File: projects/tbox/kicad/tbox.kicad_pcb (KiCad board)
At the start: 4 copper layers, 300 x 250 mm, 0 parts

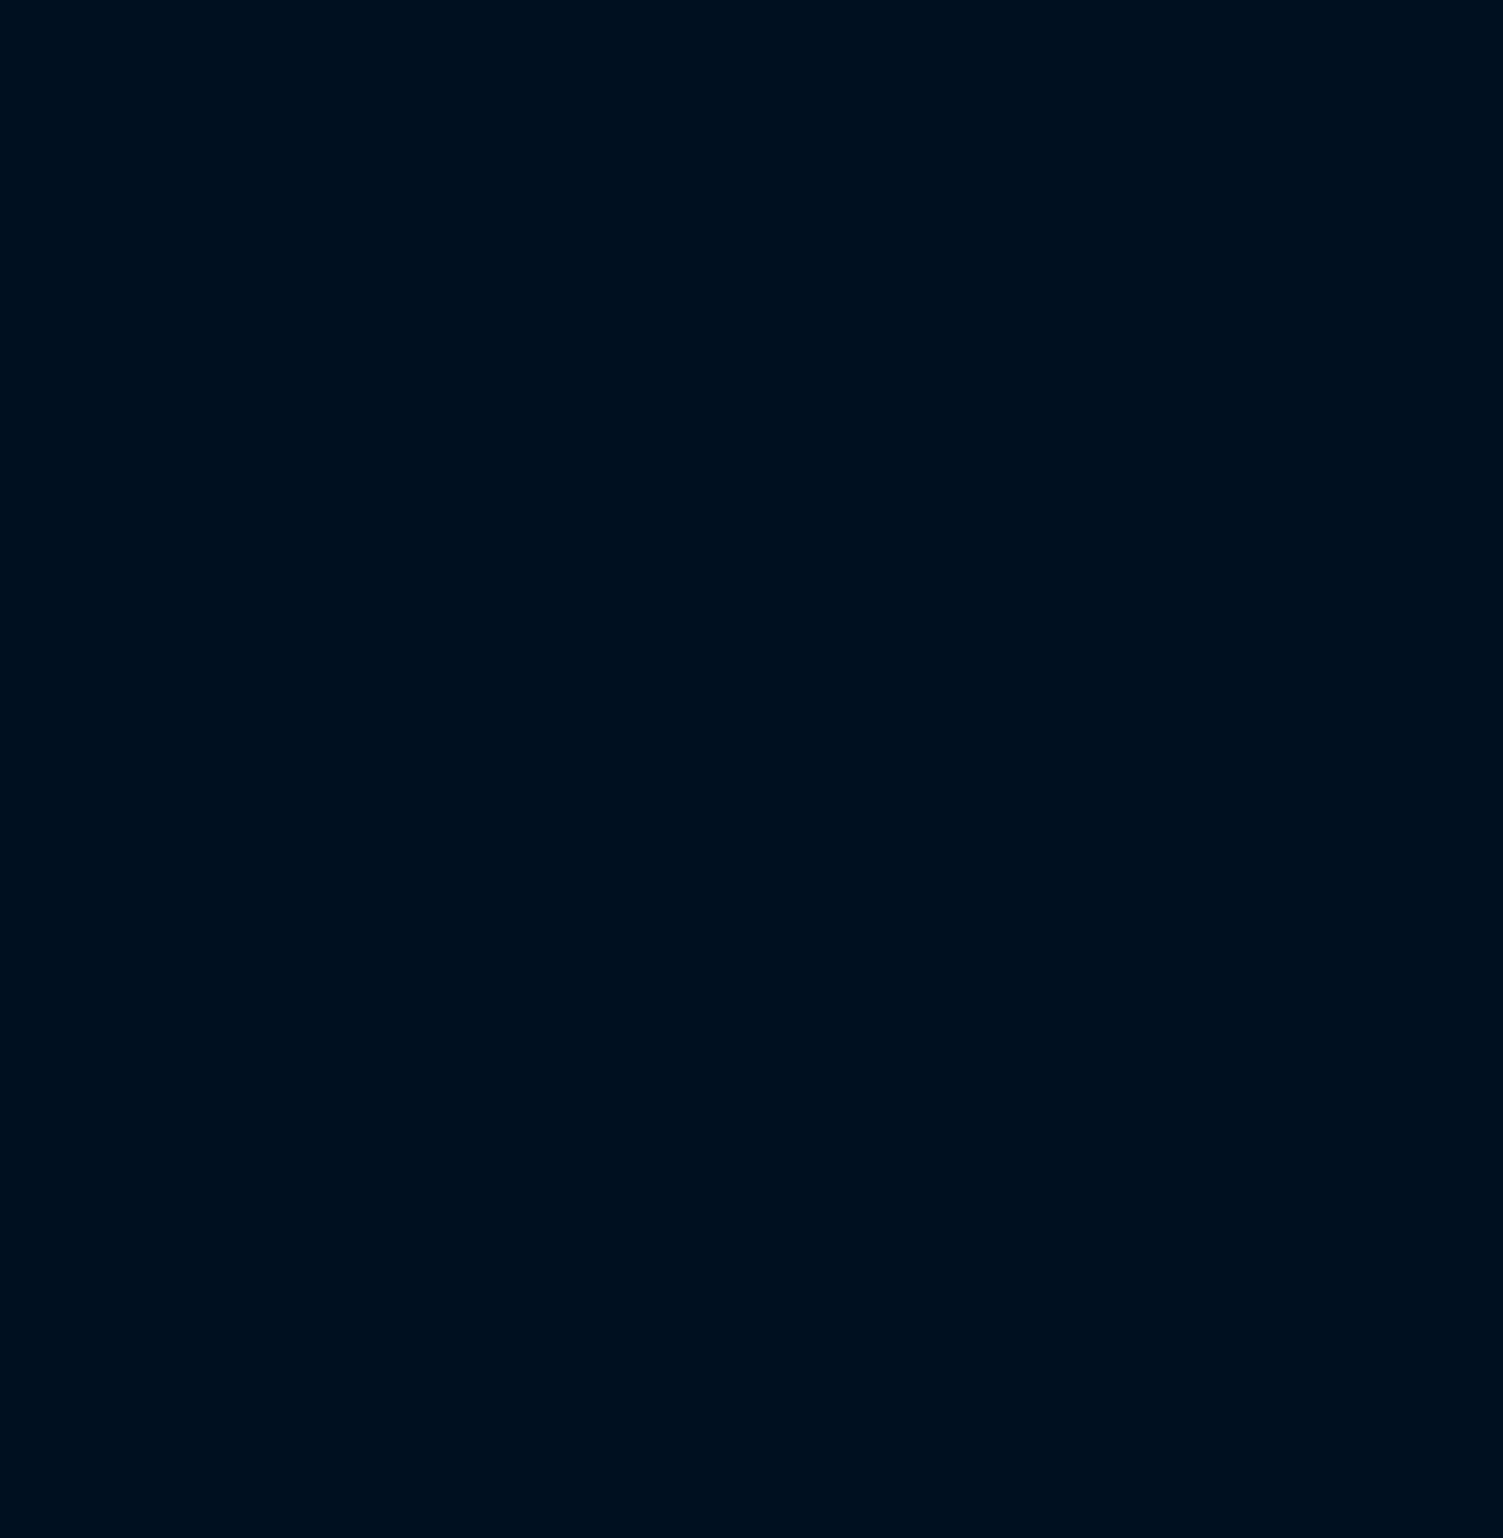
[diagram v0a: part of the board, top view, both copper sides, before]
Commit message: Footprints pulled into the panel PCB (Update PCB from Schematic)
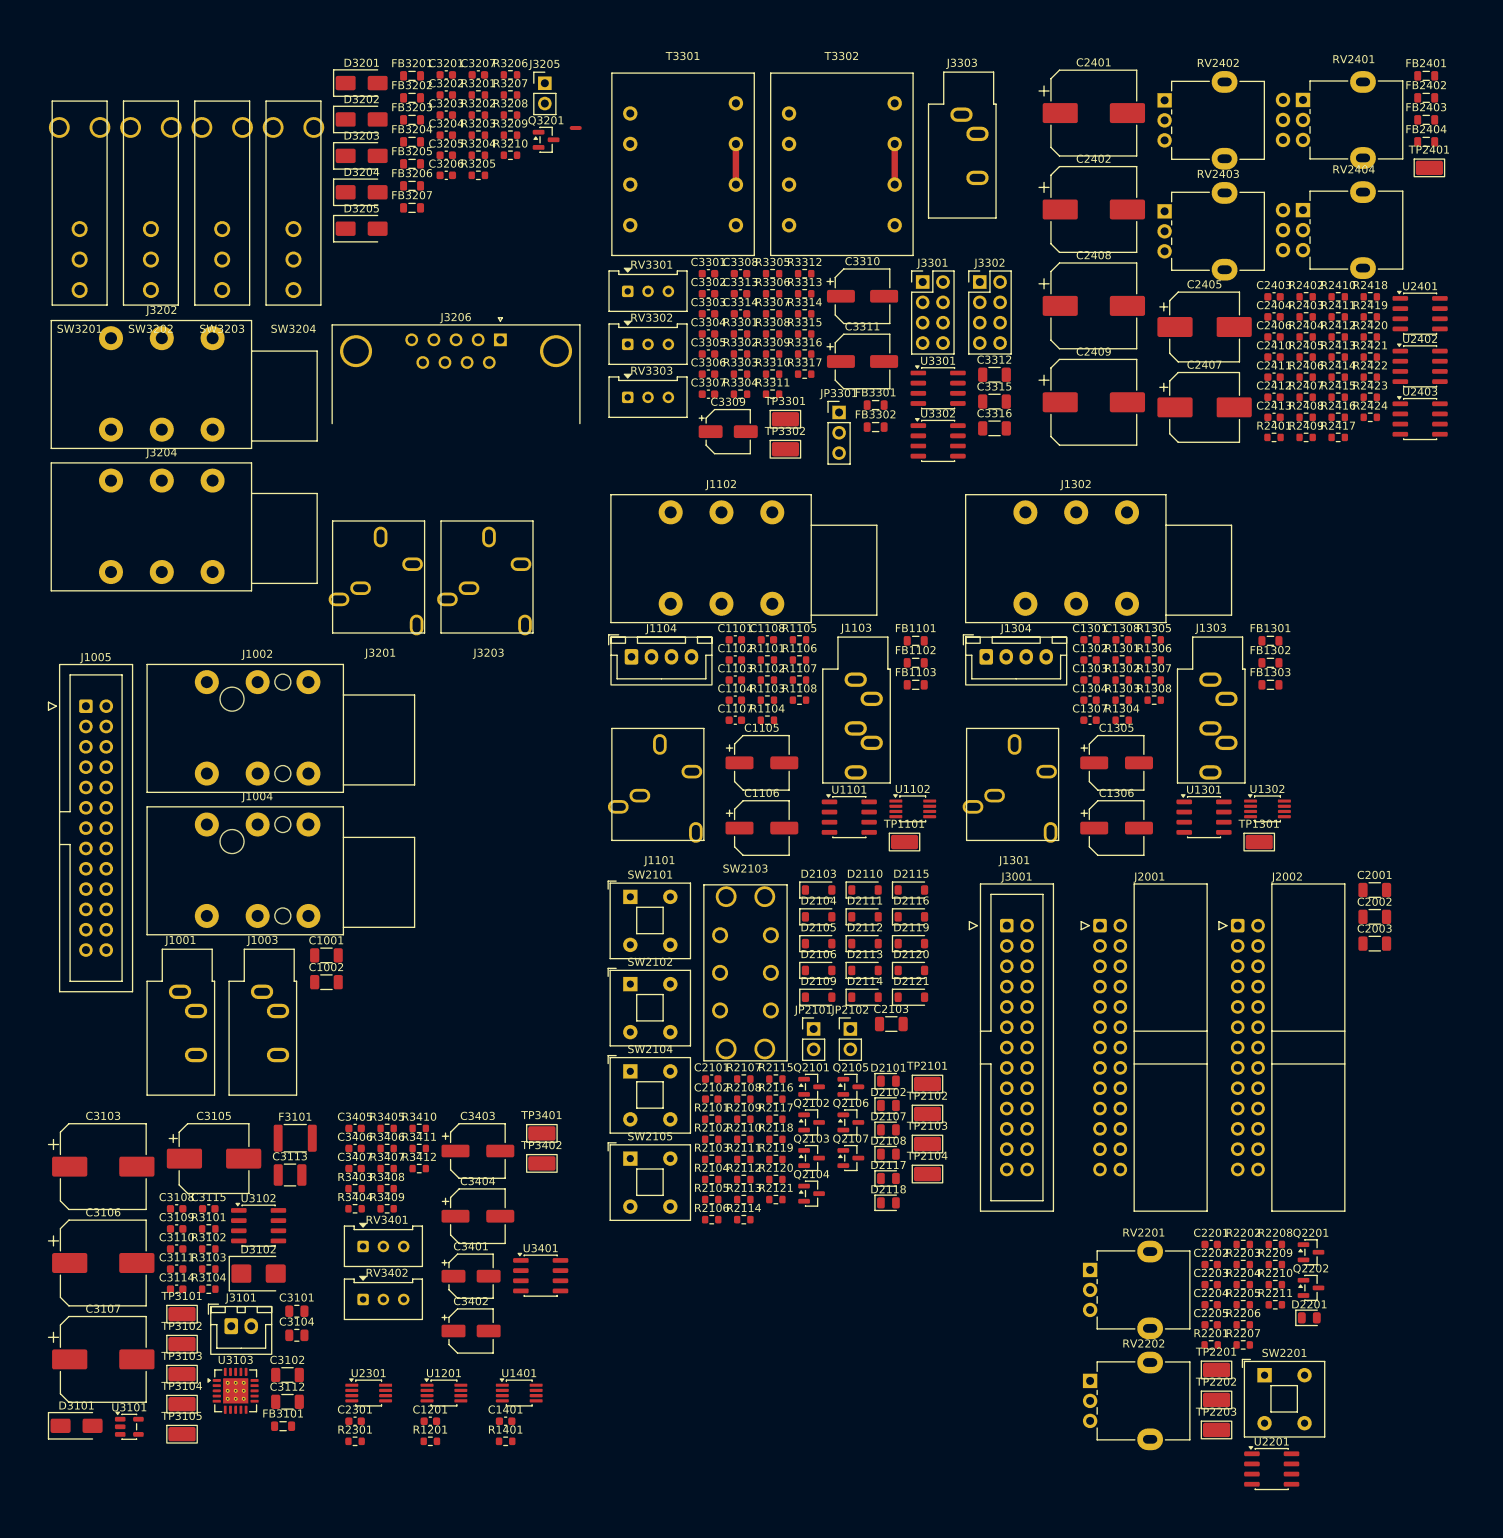
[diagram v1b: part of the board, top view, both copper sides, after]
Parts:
- added C1001: 10u, Capacitor_SMD:C_1206_3216Metric, F.Cu at (92.1, 162.8)
- added C1002: 10u, Capacitor_SMD:C_1206_3216Metric, F.Cu at (92.1, 166.2)
- added C1101: 1n, Capacitor_SMD:C_0603_1608Metric, F.Cu at (143.2, 123.4)
- added C1102: 100n, Capacitor_SMD:C_0603_1608Metric, F.Cu at (143.2, 125.9)
- added C1103: 1u, Capacitor_SMD:C_0603_1608Metric, F.Cu at (143.2, 128.4)
- added C1104: 100p, Capacitor_SMD:C_0603_1608Metric, F.Cu at (143.2, 130.9)
- added C1105: 47u, Capacitor_SMD:CP_Elec_6.3x5.4, F.Cu at (146.5, 138.7)
- added C1106: 47u, Capacitor_SMD:CP_Elec_6.3x5.4, F.Cu at (146.5, 146.9)
- added C1107: 100n, Capacitor_SMD:C_0603_1608Metric, F.Cu at (143.2, 133.4)
- added C1108: 100n, Capacitor_SMD:C_0603_1608Metric, F.Cu at (147.2, 123.4)
- added C1201: 100n, Capacitor_SMD:C_0603_1608Metric, F.Cu at (105.0, 221.0)
- added C1301: 1n, Capacitor_SMD:C_0603_1608Metric, F.Cu at (187.5, 123.4)
- added C1302: 100n, Capacitor_SMD:C_0603_1608Metric, F.Cu at (187.5, 125.9)
- added C1303: 1u, Capacitor_SMD:C_0603_1608Metric, F.Cu at (187.5, 128.4)
- added C1304: 100p, Capacitor_SMD:C_0603_1608Metric, F.Cu at (187.5, 130.9)
- added C1305: 47u, Capacitor_SMD:CP_Elec_6.3x5.4, F.Cu at (190.8, 138.7)
- added C1306: 47u, Capacitor_SMD:CP_Elec_6.3x5.4, F.Cu at (190.8, 146.9)
- added C1307: 100n, Capacitor_SMD:C_0603_1608Metric, F.Cu at (187.5, 133.4)
- added C1308: 100n, Capacitor_SMD:C_0603_1608Metric, F.Cu at (191.5, 123.4)
- added C1401: 100n, Capacitor_SMD:C_0603_1608Metric, F.Cu at (114.5, 221.0)
- added C2001: 10u, Capacitor_SMD:C_1206_3216Metric, F.Cu at (223.1, 154.6)
- added C2002: 10u, Capacitor_SMD:C_1206_3216Metric, F.Cu at (223.1, 158.0)
- added C2003: 10u, Capacitor_SMD:C_1206_3216Metric, F.Cu at (223.1, 161.3)
- added C2101: 100n, Capacitor_SMD:C_0603_1608Metric, F.Cu at (140.2, 178.3)
- added C2102: 100n, Capacitor_SMD:C_0603_1608Metric, F.Cu at (140.2, 180.8)
- added C2103: 10u, Capacitor_SMD:C_1206_3216Metric, F.Cu at (162.7, 171.4)
- added C2201: 1u, Capacitor_SMD:C_0603_1608Metric, F.Cu at (202.6, 199.0)
- added C2202: 1u, Capacitor_SMD:C_0603_1608Metric, F.Cu at (202.6, 201.5)
- added C2203: 100n, Capacitor_SMD:C_0603_1608Metric, F.Cu at (202.6, 204.0)
- added C2204: 47p, Capacitor_SMD:C_0603_1608Metric, F.Cu at (202.6, 206.5)
- added C2205: 100n, Capacitor_SMD:C_0603_1608Metric, F.Cu at (202.6, 209.0)
- added C2301: 100n, Capacitor_SMD:C_0603_1608Metric, F.Cu at (95.6, 221.0)
- added C2401: 470u, Capacitor_SMD:CP_Elec_10x10.5, F.Cu at (188.0, 57.5)
- added C2402: 470u, Capacitor_SMD:CP_Elec_10x10.5, F.Cu at (188.0, 69.6)
- added C2403: 10n, Capacitor_SMD:C_0603_1608Metric, F.Cu at (210.5, 80.5)
- added C2404: 10n, Capacitor_SMD:C_0603_1608Metric, F.Cu at (210.5, 83.0)
- added C2405: 220u, Capacitor_SMD:CP_Elec_8x10.5, F.Cu at (201.8, 84.3)
- added C2406: 100n, Capacitor_SMD:C_0603_1608Metric, F.Cu at (210.5, 85.5)
- added C2407: 220u, Capacitor_SMD:CP_Elec_8x10.5, F.Cu at (201.8, 94.3)
- added C2408: 470u, Capacitor_SMD:CP_Elec_10x10.5, F.Cu at (188.0, 81.6)
- added C2409: 470u, Capacitor_SMD:CP_Elec_10x10.5, F.Cu at (188.0, 93.7)
- added C2410: 100n, Capacitor_SMD:C_0603_1608Metric, F.Cu at (210.5, 88.0)
- added C2411: 10n, Capacitor_SMD:C_0603_1608Metric, F.Cu at (210.5, 90.5)
- added C2412: 10n, Capacitor_SMD:C_0603_1608Metric, F.Cu at (210.5, 93.0)
- added C2413: 100n, Capacitor_SMD:C_0603_1608Metric, F.Cu at (210.5, 95.6)
- added C3101: 4u7, Capacitor_SMD:C_0805_2012Metric, F.Cu at (88.4, 207.3)
- added C3102: 10u, Capacitor_SMD:C_1206_3216Metric, F.Cu at (87.2, 215.3)
- added C3103: 220u 35V, Capacitor_SMD:CP_Elec_10x10.5, F.Cu at (64.2, 189.2)
- added C3104: 4u7, Capacitor_SMD:C_0805_2012Metric, F.Cu at (88.4, 210.3)
- added C3105: 220u, Capacitor_SMD:CP_Elec_8x10.5, F.Cu at (78.0, 188.2)
- added C3106: 220u 35V, Capacitor_SMD:CP_Elec_10x10.5, F.Cu at (64.2, 201.3)
- added C3107: 470u, Capacitor_SMD:CP_Elec_10x10.5, F.Cu at (64.2, 213.3)
- added C3108: 100n, Capacitor_SMD:C_0603_1608Metric, F.Cu at (73.3, 194.5)
- added C3109: 100n, Capacitor_SMD:C_0603_1608Metric, F.Cu at (73.3, 197.0)
- added C3110: 1n, Capacitor_SMD:C_0603_1608Metric, F.Cu at (73.3, 199.5)
- added C3111: 100n, Capacitor_SMD:C_0603_1608Metric, F.Cu at (73.3, 202.0)
- added C3112: 10u, Capacitor_SMD:C_1206_3216Metric, F.Cu at (87.2, 218.6)
- added C3113: 47u X7R, Capacitor_SMD:C_1210_3225Metric, F.Cu at (87.5, 190.3)
- added C3114: 1u, Capacitor_SMD:C_0603_1608Metric, F.Cu at (73.3, 204.5)
- added C3115: 100n, Capacitor_SMD:C_0603_1608Metric, F.Cu at (77.3, 194.5)
- added C3201: 10n, Capacitor_SMD:C_0603_1608Metric, F.Cu at (107.0, 52.8)
- added C3202: 10n, Capacitor_SMD:C_0603_1608Metric, F.Cu at (107.0, 55.3)
- added C3203: 1n, Capacitor_SMD:C_0603_1608Metric, F.Cu at (107.0, 57.8)
- added C3204: 1n, Capacitor_SMD:C_0603_1608Metric, F.Cu at (107.0, 60.3)
- added C3205: 1n, Capacitor_SMD:C_0603_1608Metric, F.Cu at (107.0, 62.8)
- added C3206: 10n, Capacitor_SMD:C_0603_1608Metric, F.Cu at (107.0, 65.3)
- added C3207: 10n, Capacitor_SMD:C_0603_1608Metric, F.Cu at (111.0, 52.8)
- added C3301: 100n, Capacitor_SMD:C_0603_1608Metric, F.Cu at (139.8, 77.6)
- added C3302: 100n, Capacitor_SMD:C_0603_1608Metric, F.Cu at (139.8, 80.1)
- added C3303: 1u, Capacitor_SMD:C_0603_1608Metric, F.Cu at (139.8, 82.6)
- added C3304: 100p, Capacitor_SMD:C_0603_1608Metric, F.Cu at (139.8, 85.1)
- added C3305: 1u, Capacitor_SMD:C_0603_1608Metric, F.Cu at (139.8, 87.6)
- added C3306: 1u, Capacitor_SMD:C_0603_1608Metric, F.Cu at (139.8, 90.2)
- added C3307: 100p, Capacitor_SMD:C_0603_1608Metric, F.Cu at (139.8, 92.7)
- added C3308: 100p, Capacitor_SMD:C_0603_1608Metric, F.Cu at (143.8, 77.6)
- added C3309: 10u, Capacitor_SMD:CP_Elec_5x5.4, F.Cu at (142.3, 97.3)
- added C3310: 100u, Capacitor_SMD:CP_Elec_6.3x7.7, F.Cu at (159.1, 80.4)
- added C3311: 100u, Capacitor_SMD:CP_Elec_6.3x7.7, F.Cu at (159.1, 88.6)
- added C3312: 10u NP, Capacitor_SMD:C_1206_3216Metric, F.Cu at (175.6, 90.2)
- added C3313: 1n, Capacitor_SMD:C_0603_1608Metric, F.Cu at (143.8, 80.1)
- added C3314: 1n, Capacitor_SMD:C_0603_1608Metric, F.Cu at (143.8, 82.6)
- added C3315: 10u NP, Capacitor_SMD:C_1206_3216Metric, F.Cu at (175.6, 93.6)
- added C3316: 10u NP, Capacitor_SMD:C_1206_3216Metric, F.Cu at (175.6, 96.9)
- added C3401: 10u, Capacitor_SMD:CP_Elec_5x5.4, F.Cu at (110.1, 202.9)
- added C3402: 10u, Capacitor_SMD:CP_Elec_5x5.4, F.Cu at (110.1, 209.8)
- added C3403: 47u, Capacitor_SMD:CP_Elec_6.3x5.4, F.Cu at (111.0, 187.3)
- added C3404: 47u, Capacitor_SMD:CP_Elec_6.3x5.4, F.Cu at (111.0, 195.4)
- added C3405: 100p, Capacitor_SMD:C_0603_1608Metric, F.Cu at (95.6, 184.4)
- added C3406: 100p, Capacitor_SMD:C_0603_1608Metric, F.Cu at (95.6, 187.0)
- added C3407: 100n, Capacitor_SMD:C_0603_1608Metric, F.Cu at (95.6, 189.5)
- added D2101: TX, LED_SMD:LED_0805_2012Metric, F.Cu at (162.3, 178.5)
- added D2102: PTT A, LED_SMD:LED_0805_2012Metric, F.Cu at (162.3, 181.6)
- added D2103: 1N4148W, Diode_SMD:D_SOD-123, F.Cu at (153.6, 154.6)
- added D2104: 1N4148W, Diode_SMD:D_SOD-123, F.Cu at (153.6, 158.0)
- added D2105: 1N4148W, Diode_SMD:D_SOD-123, F.Cu at (153.6, 161.3)
- added D2106: 1N4148W, Diode_SMD:D_SOD-123, F.Cu at (153.6, 164.7)
- added D2107: PTT B, LED_SMD:LED_0805_2012Metric, F.Cu at (162.3, 184.6)
- added D2108: MUTE A, LED_SMD:LED_0805_2012Metric, F.Cu at (162.3, 187.7)
- added D2109: 1N4148W, Diode_SMD:D_SOD-123, F.Cu at (153.6, 168.0)
- added D2110: 1N4148W, Diode_SMD:D_SOD-123, F.Cu at (159.4, 154.6)
- added D2111: 1N4148W, Diode_SMD:D_SOD-123, F.Cu at (159.4, 158.0)
- added D2112: 1N4148W, Diode_SMD:D_SOD-123, F.Cu at (159.4, 161.3)
- added D2113: 1N4148W, Diode_SMD:D_SOD-123, F.Cu at (159.4, 164.7)
- added D2114: 1N4148W, Diode_SMD:D_SOD-123, F.Cu at (159.4, 168.0)
- added D2115: 1N4148W, Diode_SMD:D_SOD-123, F.Cu at (165.2, 154.6)
- added D2116: 1N4148W, Diode_SMD:D_SOD-123, F.Cu at (165.2, 158.0)
- added D2117: MUTE B, LED_SMD:LED_0805_2012Metric, F.Cu at (162.3, 190.7)
- added D2118: PWR, LED_SMD:LED_0805_2012Metric, F.Cu at (162.3, 193.7)
- added D2119: 1N4148W, Diode_SMD:D_SOD-123, F.Cu at (165.2, 161.3)
- added D2120: 1N4148W, Diode_SMD:D_SOD-123, F.Cu at (165.2, 164.7)
- added D2121: 1N4148W, Diode_SMD:D_SOD-123, F.Cu at (165.2, 168.0)
- added D2201: IC LED, LED_SMD:LED_0805_2012Metric, F.Cu at (214.9, 208.1)
- added D3101: SS34, Diode_SMD:D_SMA, F.Cu at (60.8, 221.6)
- added D3102: SMBJ18A, Diode_SMD:D_SMB, F.Cu at (83.6, 202.6)
- added D3201: SMAJ15CA, Diode_SMD:D_SMA, F.Cu at (96.5, 53.8)
- added D3202: SMAJ15CA, Diode_SMD:D_SMA, F.Cu at (96.5, 58.3)
- added D3203: SMAJ15CA, Diode_SMD:D_SMA, F.Cu at (96.5, 62.9)
- added D3204: SMAJ15A, Diode_SMD:D_SMA, F.Cu at (96.5, 67.4)
- added D3205: SMAJ15A, Diode_SMD:D_SMA, F.Cu at (96.5, 72.0)
- added F3101: PTC 500mA, Fuse:Fuse_1812_4532Metric, F.Cu at (88.2, 185.7)
- added FB1101: 600R, Inductor_SMD:L_0805_2012Metric, F.Cu at (165.7, 123.5)
- added FB1102: 600R, Inductor_SMD:L_0805_2012Metric, F.Cu at (165.7, 126.2)
- added FB1103: 600R, Inductor_SMD:L_0805_2012Metric, F.Cu at (165.7, 129.0)
- added FB1301: 600R, Inductor_SMD:L_0805_2012Metric, F.Cu at (210.1, 123.5)
- added FB1302: 600R, Inductor_SMD:L_0805_2012Metric, F.Cu at (210.1, 126.2)
- added FB1303: 600R, Inductor_SMD:L_0805_2012Metric, F.Cu at (210.1, 129.0)
- added FB2401: 600R, Inductor_SMD:L_0805_2012Metric, F.Cu at (229.5, 52.9)
- added FB2402: 600R, Inductor_SMD:L_0805_2012Metric, F.Cu at (229.5, 55.6)
- added FB2403: 600R, Inductor_SMD:L_0805_2012Metric, F.Cu at (229.5, 58.4)
- added FB2404: 600R, Inductor_SMD:L_0805_2012Metric, F.Cu at (229.5, 61.1)
- added FB3101: 600R, Inductor_SMD:L_0805_2012Metric, F.Cu at (86.6, 221.7)
- added FB3201: 600R, Inductor_SMD:L_0805_2012Metric, F.Cu at (102.8, 52.9)
- added FB3202: 600R, Inductor_SMD:L_0805_2012Metric, F.Cu at (102.8, 55.6)
- added FB3203: 600R, Inductor_SMD:L_0805_2012Metric, F.Cu at (102.8, 58.4)
- added FB3204: 600R, Inductor_SMD:L_0805_2012Metric, F.Cu at (102.8, 61.1)
- added FB3205: 600R, Inductor_SMD:L_0805_2012Metric, F.Cu at (102.8, 63.9)
- added FB3206: 600R, Inductor_SMD:L_0805_2012Metric, F.Cu at (102.8, 66.6)
- added FB3207: 600R, Inductor_SMD:L_0805_2012Metric, F.Cu at (102.8, 69.4)
- added FB3301: 600R, Inductor_SMD:L_0805_2012Metric, F.Cu at (160.7, 94.0)
- added FB3302: 600R, Inductor_SMD:L_0805_2012Metric, F.Cu at (160.7, 96.8)
- added J1001: PHONES A 3.5, Connector_Audio:Jack_3.5mm_CUI_SJ1-3533NG_Horizontal, F.Cu at (73.8, 167.4)
- added J1002: PHONES A 1/4, Connector_Audio:Jack_6.35mm_Neutrik_NRJ6HF-1_Horizontal, F.Cu at (77.1, 128.7)
- added J1003: PHONES B 3.5, Connector_Audio:Jack_3.5mm_CUI_SJ1-3533NG_Horizontal, F.Cu at (84.0, 167.4)
- added J1004: PHONES B 1/4, Connector_Audio:Jack_6.35mm_Neutrik_NRJ6HF-1_Horizontal, F.Cu at (77.1, 146.5)
- added J1005: TO CTRL J2001, Connector_IDC:IDC-Header_2x13_P2.54mm_Vertical, F.Cu at (62.0, 131.7)
- added J1101: MIC 3.5, tbox:Jack_3.5mm_Switchcraft_35RAPCxxH3_Horizontal, F.Cu at (133.7, 134.4)
- added J1102: MIC 1/4, Connector_Audio:Jack_6.35mm_Neutrik_NRJ6HM-1-PRE_Horizontal, F.Cu at (135.1, 107.4)
- added J1103: HEADSET, Connector_Audio:Jack_3.5mm_CUI_SJ1-3535NG_Horizontal, F.Cu at (158.2, 128.3)
- added J1104: SPARE, Connector_JST:JST_XH_B4B-XH-A_1x04_P2.50mm_Vertical, F.Cu at (130.2, 125.5)
- added J1301: MIC 3.5, tbox:Jack_3.5mm_Switchcraft_35RAPCxxH3_Horizontal, F.Cu at (178.1, 134.4)
- added J1302: MIC 1/4, Connector_Audio:Jack_6.35mm_Neutrik_NRJ6HM-1-PRE_Horizontal, F.Cu at (179.4, 107.4)
- added J1303: HEADSET, Connector_Audio:Jack_3.5mm_CUI_SJ1-3535NG_Horizontal, F.Cu at (202.6, 128.3)
- added J1304: SPARE, Connector_JST:JST_XH_B4B-XH-A_1x04_P2.50mm_Vertical, F.Cu at (174.5, 125.5)
- added J2001: TO FRONT J1005, Connector_IDC:IDC-Header_2x13_P2.54mm_Horizontal, F.Cu at (188.8, 159.1)
- added J2002: TO REAR J3001, Connector_IDC:IDC-Header_2x13_P2.54mm_Horizontal, F.Cu at (206.0, 159.1)
- added J3001: TO CTRL J2002, Connector_IDC:IDC-Header_2x13_P2.54mm_Vertical, F.Cu at (177.1, 159.1)
- added J3101: PWR IN (panel Powerpole), Connector_JST:JST_XH_B2B-XH-A_1x02_P2.50mm_Vertical, F.Cu at (80.2, 209.2)
- added J3201: PTT A 3.5, tbox:Jack_3.5mm_Switchcraft_35RAPCxxH3_Horizontal, F.Cu at (98.8, 108.5)
- added J3202: PTT A 1/4, Connector_Audio:Jack_6.35mm_Neutrik_NRJ6HM-1-PRE_Horizontal, F.Cu at (65.1, 85.7)
- added J3203: PTT B 3.5, tbox:Jack_3.5mm_Switchcraft_35RAPCxxH3_Horizontal, F.Cu at (112.4, 108.5)
- added J3204: PTT B 1/4, Connector_Audio:Jack_6.35mm_Neutrik_NRJ6HM-1-PRE_Horizontal, F.Cu at (65.1, 103.5)
- added J3205: CW SPARE, Connector_PinHeader_2.54mm:PinHeader_1x02_P2.54mm_Vertical, F.Cu at (119.4, 53.8)
- added J3206: RIG DE-9, Connector_Dsub:DSUB-9_Socket_Horizontal_P2.77x2.84mm_EdgePinOffset7.70mm_Housed_MountingHolesOffset9.12mm, F.Cu at (113.8, 85.9)
- added J3301: LINE L SRC, Connector_PinHeader_2.54mm:PinHeader_2x04_P2.54mm_Vertical, F.Cu at (166.6, 78.6)
- added J3302: LINE R SRC, Connector_PinHeader_2.54mm:PinHeader_2x04_P2.54mm_Vertical, F.Cu at (173.7, 78.6)
- added J3303: LINE OUT, Connector_Audio:Jack_3.5mm_CUI_SJ1-3533NG_Horizontal, F.Cu at (171.4, 57.7)
- added JP2101: PTT GATE, Connector_PinHeader_2.54mm:PinHeader_1x02_P2.54mm_Vertical, F.Cu at (153.0, 172.0)
- added JP2102: PTT GATE, Connector_PinHeader_2.54mm:PinHeader_1x02_P2.54mm_Vertical, F.Cu at (157.5, 172.0)
- added JP3301: MIC/LINE, Connector_PinHeader_2.54mm:PinHeader_1x03_P2.54mm_Vertical, F.Cu at (156.1, 94.9)
- added NT3201: CHASSIS-GND tie, NetTie:NetTie-2_SMD_Pad0.5mm, F.Cu at (123.2, 59.4)
- added Q2101: 2N7002, Package_TO_SOT_SMD:SOT-23, F.Cu at (152.7, 179.2)
- added Q2102: 2N7002, Package_TO_SOT_SMD:SOT-23, F.Cu at (152.7, 183.7)
- added Q2103: 2N7002, Package_TO_SOT_SMD:SOT-23, F.Cu at (152.7, 188.1)
- added Q2104: 2N7002, Package_TO_SOT_SMD:SOT-23, F.Cu at (152.7, 192.6)
- added Q2105: 2N7002, Package_TO_SOT_SMD:SOT-23, F.Cu at (157.6, 179.2)
- added Q2106: 2N7002, Package_TO_SOT_SMD:SOT-23, F.Cu at (157.6, 183.7)
- added Q2107: 2N7002, Package_TO_SOT_SMD:SOT-23, F.Cu at (157.6, 188.1)
- added Q2201: MMBT3904, Package_TO_SOT_SMD:SOT-23, F.Cu at (215.1, 199.9)
- added Q2202: 2N7002, Package_TO_SOT_SMD:SOT-23, F.Cu at (215.1, 204.4)
- added Q3201: 2N7002, Package_TO_SOT_SMD:SOT-23, F.Cu at (119.5, 60.9)
- added R1101: 2k2, Resistor_SMD:R_0603_1608Metric, F.Cu at (147.2, 125.9)
- added R1102: 47k, Resistor_SMD:R_0603_1608Metric, F.Cu at (147.2, 128.4)
- added R1103: 100R, Resistor_SMD:R_0603_1608Metric, F.Cu at (147.2, 130.9)
- added R1104: 1k1, Resistor_SMD:R_0603_1608Metric, F.Cu at (147.2, 133.4)
- added R1105: 10k, Resistor_SMD:R_0603_1608Metric, F.Cu at (151.2, 123.4)
- added R1106: 1k1, Resistor_SMD:R_0603_1608Metric, F.Cu at (151.2, 125.9)
- added R1107: 10k, Resistor_SMD:R_0603_1608Metric, F.Cu at (151.2, 128.4)
- added R1108: 100k, Resistor_SMD:R_0603_1608Metric, F.Cu at (151.2, 130.9)
- added R1201: 1M, Resistor_SMD:R_0603_1608Metric, F.Cu at (105.0, 223.6)
- added R1301: 2k2, Resistor_SMD:R_0603_1608Metric, F.Cu at (191.5, 125.9)
- added R1302: 47k, Resistor_SMD:R_0603_1608Metric, F.Cu at (191.5, 128.4)
- added R1303: 100R, Resistor_SMD:R_0603_1608Metric, F.Cu at (191.5, 130.9)
- added R1304: 1k1, Resistor_SMD:R_0603_1608Metric, F.Cu at (191.5, 133.4)
- added R1305: 10k, Resistor_SMD:R_0603_1608Metric, F.Cu at (195.5, 123.4)
- added R1306: 1k1, Resistor_SMD:R_0603_1608Metric, F.Cu at (195.5, 125.9)
- added R1307: 10k, Resistor_SMD:R_0603_1608Metric, F.Cu at (195.5, 128.4)
- added R1308: 100k, Resistor_SMD:R_0603_1608Metric, F.Cu at (195.5, 130.9)
- added R1401: 1M, Resistor_SMD:R_0603_1608Metric, F.Cu at (114.5, 223.6)
- added R2101: 10k, Resistor_SMD:R_0603_1608Metric, F.Cu at (140.2, 183.3)
- added R2102: 680R, Resistor_SMD:R_0603_1608Metric, F.Cu at (140.2, 185.8)
- added R2103: 10k, Resistor_SMD:R_0603_1608Metric, F.Cu at (140.2, 188.3)
- added R2104: 1k, Resistor_SMD:R_0603_1608Metric, F.Cu at (140.2, 190.8)
- added R2105: 1k, Resistor_SMD:R_0603_1608Metric, F.Cu at (140.2, 193.3)
- added R2106: 2k2, Resistor_SMD:R_0603_1608Metric, F.Cu at (140.2, 195.8)
- added R2107: 10k, Resistor_SMD:R_0603_1608Metric, F.Cu at (144.2, 178.3)
- added R2108: 10k, Resistor_SMD:R_0603_1608Metric, F.Cu at (144.2, 180.8)
- added R2109: 10k, Resistor_SMD:R_0603_1608Metric, F.Cu at (144.2, 183.3)
- added R2110: 2k2, Resistor_SMD:R_0603_1608Metric, F.Cu at (144.2, 185.8)
- added R2111: 2k2, Resistor_SMD:R_0603_1608Metric, F.Cu at (144.2, 188.3)
- added R2112: 2k2, Resistor_SMD:R_0603_1608Metric, F.Cu at (144.2, 190.8)
- added R2113: 10k, Resistor_SMD:R_0603_1608Metric, F.Cu at (144.2, 193.3)
- added R2114: 2k2, Resistor_SMD:R_0603_1608Metric, F.Cu at (144.2, 195.8)
- added R2115: 1k, Resistor_SMD:R_0603_1608Metric, F.Cu at (148.2, 178.3)
- added R2116: 1k, Resistor_SMD:R_0603_1608Metric, F.Cu at (148.2, 180.8)
- added R2117: 47k, Resistor_SMD:R_0603_1608Metric, F.Cu at (148.2, 183.3)
- added R2118: 10k, Resistor_SMD:R_0603_1608Metric, F.Cu at (148.2, 185.8)
- added R2119: 2k2, Resistor_SMD:R_0603_1608Metric, F.Cu at (148.2, 188.3)
- added R2120: 2k2, Resistor_SMD:R_0603_1608Metric, F.Cu at (148.2, 190.8)
- added R2121: 470k, Resistor_SMD:R_0603_1608Metric, F.Cu at (148.2, 193.3)
- added R2201: 10k, Resistor_SMD:R_0603_1608Metric, F.Cu at (202.6, 211.5)
- added R2202: 10k, Resistor_SMD:R_0603_1608Metric, F.Cu at (206.7, 199.0)
- added R2203: 10k, Resistor_SMD:R_0603_1608Metric, F.Cu at (206.7, 201.5)
- added R2204: 10k, Resistor_SMD:R_0603_1608Metric, F.Cu at (206.7, 204.0)
- added R2205: 20k, Resistor_SMD:R_0603_1608Metric, F.Cu at (206.7, 206.5)
- added R2206: 10k, Resistor_SMD:R_0603_1608Metric, F.Cu at (206.7, 209.0)
- added R2207: 100R, Resistor_SMD:R_0603_1608Metric, F.Cu at (206.7, 211.5)
- added R2208: 10k, Resistor_SMD:R_0603_1608Metric, F.Cu at (210.7, 199.0)
- added R2209: 10k, Resistor_SMD:R_0603_1608Metric, F.Cu at (210.7, 201.5)
- added R2210: 2k2, Resistor_SMD:R_0603_1608Metric, F.Cu at (210.7, 204.0)
- added R2211: 100k, Resistor_SMD:R_0603_1608Metric, F.Cu at (210.7, 206.5)
- added R2301: 1M, Resistor_SMD:R_0603_1608Metric, F.Cu at (95.6, 223.6)
- added R2401: 10k, Resistor_SMD:R_0603_1608Metric, F.Cu at (210.5, 98.1)
- added R2402: 10k, Resistor_SMD:R_0603_1608Metric, F.Cu at (214.5, 80.5)
- added R2403: 10k, Resistor_SMD:R_0603_1608Metric, F.Cu at (214.5, 83.0)
- added R2404: 10k, Resistor_SMD:R_0603_1608Metric, F.Cu at (214.5, 85.5)
- added R2405: 10k, Resistor_SMD:R_0603_1608Metric, F.Cu at (214.5, 88.0)
- added R2406: 10k, Resistor_SMD:R_0603_1608Metric, F.Cu at (214.5, 90.5)
- added R2407: 150k, Resistor_SMD:R_0603_1608Metric, F.Cu at (214.5, 93.0)
- added R2408: 150k, Resistor_SMD:R_0603_1608Metric, F.Cu at (214.5, 95.6)
- added R2409: 10R, Resistor_SMD:R_0603_1608Metric, F.Cu at (214.5, 98.1)
- added R2410: 10R, Resistor_SMD:R_0603_1608Metric, F.Cu at (218.5, 80.5)
- added R2411: 4k7, Resistor_SMD:R_0603_1608Metric, F.Cu at (218.5, 83.0)
- added R2412: 4k7, Resistor_SMD:R_0603_1608Metric, F.Cu at (218.5, 85.5)
- added R2413: 10k, Resistor_SMD:R_0603_1608Metric, F.Cu at (218.5, 88.0)
- added R2414: 10k, Resistor_SMD:R_0603_1608Metric, F.Cu at (218.5, 90.5)
- added R2415: 10k, Resistor_SMD:R_0603_1608Metric, F.Cu at (218.5, 93.0)
- added R2416: 10k, Resistor_SMD:R_0603_1608Metric, F.Cu at (218.5, 95.6)
- added R2417: 10k, Resistor_SMD:R_0603_1608Metric, F.Cu at (218.5, 98.1)
- added R2418: 10k, Resistor_SMD:R_0603_1608Metric, F.Cu at (222.5, 80.5)
- added R2419: 150k, Resistor_SMD:R_0603_1608Metric, F.Cu at (222.5, 83.0)
- added R2420: 150k, Resistor_SMD:R_0603_1608Metric, F.Cu at (222.5, 85.5)
- added R2421: 10R, Resistor_SMD:R_0603_1608Metric, F.Cu at (222.5, 88.0)
- added R2422: 10R, Resistor_SMD:R_0603_1608Metric, F.Cu at (222.5, 90.5)
- added R2423: 4k7, Resistor_SMD:R_0603_1608Metric, F.Cu at (222.5, 93.0)
- added R2424: 4k7, Resistor_SMD:R_0603_1608Metric, F.Cu at (222.5, 95.6)
- added R3101: 10k, Resistor_SMD:R_0603_1608Metric, F.Cu at (77.3, 197.0)
- added R3102: 10k, Resistor_SMD:R_0603_1608Metric, F.Cu at (77.3, 199.5)
- added R3103: 47R, Resistor_SMD:R_0603_1608Metric, F.Cu at (77.3, 202.0)
- added R3104: 10R, Resistor_SMD:R_0603_1608Metric, F.Cu at (77.3, 204.5)
- added R3201: 10k, Resistor_SMD:R_0603_1608Metric, F.Cu at (111.0, 55.3)
- added R3202: 10k, Resistor_SMD:R_0603_1608Metric, F.Cu at (111.0, 57.8)
- added R3203: 100R, Resistor_SMD:R_0603_1608Metric, F.Cu at (111.0, 60.3)
- added R3204: 100R, Resistor_SMD:R_0603_1608Metric, F.Cu at (111.0, 62.8)
- added R3205: 100R, Resistor_SMD:R_0603_1608Metric, F.Cu at (111.0, 65.3)
- added R3206: 100R, Resistor_SMD:R_0603_1608Metric, F.Cu at (115.1, 52.8)
- added R3207: 100R, Resistor_SMD:R_0603_1608Metric, F.Cu at (115.1, 55.3)
- added R3208: 100R, Resistor_SMD:R_0603_1608Metric, F.Cu at (115.1, 57.8)
- added R3209: 1k, Resistor_SMD:R_0603_1608Metric, F.Cu at (115.1, 60.3)
- added R3210: 1k, Resistor_SMD:R_0603_1608Metric, F.Cu at (115.1, 62.8)
- added R3301: 22k, Resistor_SMD:R_0603_1608Metric, F.Cu at (143.8, 85.1)
- added R3302: 22k, Resistor_SMD:R_0603_1608Metric, F.Cu at (143.8, 87.6)
- added R3303: 100R, Resistor_SMD:R_0603_1608Metric, F.Cu at (143.8, 90.2)
- added R3304: 10k, Resistor_SMD:R_0603_1608Metric, F.Cu at (143.8, 92.7)
- added R3305: 10k, Resistor_SMD:R_0603_1608Metric, F.Cu at (147.8, 77.6)
- added R3306: 10k, Resistor_SMD:R_0603_1608Metric, F.Cu at (147.8, 80.1)
- added R3307: 7k5, Resistor_SMD:R_0603_1608Metric, F.Cu at (147.8, 82.6)
- added R3308: 100R, Resistor_SMD:R_0603_1608Metric, F.Cu at (147.8, 85.1)
- added R3309: 100R, Resistor_SMD:R_0603_1608Metric, F.Cu at (147.8, 87.6)
- added R3310: 100R, Resistor_SMD:R_0603_1608Metric, F.Cu at (147.8, 90.2)
- added R3311: 7k5, Resistor_SMD:R_0603_1608Metric, F.Cu at (147.8, 92.7)
- added R3312: 7k5, Resistor_SMD:R_0603_1608Metric, F.Cu at (151.8, 77.6)
- added R3313: 100R, Resistor_SMD:R_0603_1608Metric, F.Cu at (151.8, 80.1)
- added R3314: 100R, Resistor_SMD:R_0603_1608Metric, F.Cu at (151.8, 82.6)
- added R3315: 12k, Resistor_SMD:R_0603_1608Metric, F.Cu at (151.8, 85.1)
- added R3316: 620R, Resistor_SMD:R_0603_1608Metric, F.Cu at (151.8, 87.6)
- added R3317: 100k, Resistor_SMD:R_0603_1608Metric, F.Cu at (151.8, 90.2)
- added R3403: 100R, Resistor_SMD:R_0603_1608Metric, F.Cu at (95.6, 192.0)
- added R3404: 100R, Resistor_SMD:R_0603_1608Metric, F.Cu at (95.6, 194.5)
- added R3405: 10k, Resistor_SMD:R_0603_1608Metric, F.Cu at (99.6, 184.4)
- added R3406: 10k, Resistor_SMD:R_0603_1608Metric, F.Cu at (99.6, 187.0)
- added R3407: 100k, Resistor_SMD:R_0603_1608Metric, F.Cu at (99.6, 189.5)
- added R3408: 100k, Resistor_SMD:R_0603_1608Metric, F.Cu at (99.6, 192.0)
- added R3409: 47k, Resistor_SMD:R_0603_1608Metric, F.Cu at (99.6, 194.5)
- added R3410: 47k, Resistor_SMD:R_0603_1608Metric, F.Cu at (103.7, 184.4)
- added R3411: 100R, Resistor_SMD:R_0603_1608Metric, F.Cu at (103.7, 187.0)
- added R3412: 100R, Resistor_SMD:R_0603_1608Metric, F.Cu at (103.7, 189.5)
- added RV2201: 10k, Potentiometer_THT:Potentiometer_Alpha_RD901F-40-00D_Single_Vertical, F.Cu at (187.5, 202.1)
- added RV2202: 10k, Potentiometer_THT:Potentiometer_Alpha_RD901F-40-00D_Single_Vertical, F.Cu at (187.5, 216.0)
- added RV2401: 10k dual, Potentiometer_THT:Potentiometer_Alpha_RD902F-40-00D_Dual_Vertical, F.Cu at (214.1, 55.9)
- added RV2402: 10k, Potentiometer_THT:Potentiometer_Alpha_RD901F-40-00D_Single_Vertical, F.Cu at (196.8, 55.9)
- added RV2403: 10k, Potentiometer_THT:Potentiometer_Alpha_RD901F-40-00D_Single_Vertical, F.Cu at (196.8, 69.8)
- added RV2404: 10k dual, Potentiometer_THT:Potentiometer_Alpha_RD902F-40-00D_Dual_Vertical, F.Cu at (214.1, 69.7)
- added RV3301: 10k, Potentiometer_THT:Potentiometer_Bourns_3386W_Horizontal, F.Cu at (129.7, 79.8)
- added RV3302: 10k, Potentiometer_THT:Potentiometer_Bourns_3386W_Horizontal, F.Cu at (129.7, 86.4)
- added RV3303: 10k, Potentiometer_THT:Potentiometer_Bourns_3386W_Horizontal, F.Cu at (129.7, 93.1)
- added RV3401: 10k, Potentiometer_THT:Potentiometer_Bourns_3386W_Horizontal, F.Cu at (96.6, 199.2)
- added RV3402: 10k, Potentiometer_THT:Potentiometer_Bourns_3386W_Horizontal, F.Cu at (96.6, 205.8)
- added SW2101: PTT A, Button_Switch_THT:SW_Push_2P1T_Toggle_CK_PVA1xxH2xxxxxxV2, F.Cu at (130.0, 155.5)
- added SW2102: PTT B, Button_Switch_THT:SW_Push_2P1T_Toggle_CK_PVA1xxH2xxxxxxV2, F.Cu at (130.0, 166.4)
- added SW2103: OVERRIDE, tbox:SW_Toggle_CK_7201_V-Bracket_Vertical, F.Cu at (144.4, 165.0)
- added SW2104: MUTE A, Button_Switch_THT:SW_Push_2P1T_Toggle_CK_PVA1xxH2xxxxxxV2, F.Cu at (130.0, 177.3)
- added SW2105: MUTE B, Button_Switch_THT:SW_Push_2P1T_Toggle_CK_PVA1xxH2xxxxxxV2, F.Cu at (130.0, 188.2)
- added SW2201: INTERCOM, Button_Switch_THT:SW_Push_2P1T_Toggle_CK_PVA1xxH2xxxxxxV2, F.Cu at (209.3, 215.3)
- added SW3201: GAIN A HI, tbox:SW_Toggle_CK_7101_AV2_Horizontal, F.Cu at (61.2, 72.0)
- added SW3202: GAIN B HI, tbox:SW_Toggle_CK_7101_AV2_Horizontal, F.Cu at (70.1, 72.0)
- added SW3203: BIAS A, tbox:SW_Toggle_CK_7101_AV2_Horizontal, F.Cu at (79.0, 72.0)
- added SW3204: BIAS B, tbox:SW_Toggle_CK_7101_AV2_Horizontal, F.Cu at (87.9, 72.0)
- added T3301: 600R:600R, tbox:Transformer_Triad_TY-250P, F.Cu at (136.6, 63.9)
- added T3302: 600R:600R, tbox:Transformer_Triad_TY-250P, F.Cu at (156.5, 63.9)
- added TP1101: GND, TestPoint:TestPoint_Keystone_5015_Micro_Mini, F.Cu at (164.3, 148.6)
- added TP1301: GND, TestPoint:TestPoint_Keystone_5015_Micro_Mini, F.Cu at (208.7, 148.6)
- added TP2101: PTT_ACTIVE, TestPoint:TestPoint_Keystone_5015_Micro_Mini, F.Cu at (167.2, 178.9)
- added TP2102: MUTE_A, TestPoint:TestPoint_Keystone_5015_Micro_Mini, F.Cu at (167.2, 182.6)
- added TP2103: MUTE_B, TestPoint:TestPoint_Keystone_5015_Micro_Mini, F.Cu at (167.2, 186.4)
- added TP2104: GND, TestPoint:TestPoint_Keystone_5015_Micro_Mini, F.Cu at (167.2, 190.1)
- added TP2201: TX_MIX, TestPoint:TestPoint_Keystone_5015_Micro_Mini, F.Cu at (203.3, 214.6)
- added TP2202: CH_A_OUT, TestPoint:TestPoint_Keystone_5015_Micro_Mini, F.Cu at (203.3, 218.4)
- added TP2203: CH_B_OUT, TestPoint:TestPoint_Keystone_5015_Micro_Mini, F.Cu at (203.3, 222.1)
- added TP2401: GND, TestPoint:TestPoint_Keystone_5015_Micro_Mini, F.Cu at (229.9, 64.4)
- added TP3101: TestPoint, TestPoint:TestPoint_Keystone_5015_Micro_Mini, F.Cu at (74.0, 207.7)
- added TP3102: TestPoint, TestPoint:TestPoint_Keystone_5015_Micro_Mini, F.Cu at (74.0, 211.4)
- added TP3103: TestPoint, TestPoint:TestPoint_Keystone_5015_Micro_Mini, F.Cu at (74.0, 215.2)
- added TP3104: TestPoint, TestPoint:TestPoint_Keystone_5015_Micro_Mini, F.Cu at (74.0, 218.9)
- added TP3105: TestPoint, TestPoint:TestPoint_Keystone_5015_Micro_Mini, F.Cu at (74.0, 222.7)
- added TP3301: GND, TestPoint:TestPoint_Keystone_5015_Micro_Mini, F.Cu at (149.4, 95.8)
- added TP3302: MIC_OUT, TestPoint:TestPoint_Keystone_5015_Micro_Mini, F.Cu at (149.4, 99.5)
- added TP3401: RX_L_BUS, TestPoint:TestPoint_Keystone_5015_Micro_Mini, F.Cu at (119.0, 185.1)
- added TP3402: RX_R_BUS, TestPoint:TestPoint_Keystone_5015_Micro_Mini, F.Cu at (119.0, 188.8)
- added U1101: OPA1678, Package_SO:SOIC-8_3.9x4.9mm_P1.27mm, F.Cu at (157.4, 145.5)
- added U1102: TS12A12511, Package_SO:MSOP-8_3x3mm_P0.65mm, F.Cu at (165.3, 144.5)
- added U1201: TS12A12511, Package_SO:MSOP-8_3x3mm_P0.65mm, F.Cu at (106.7, 217.5)
- added U1301: OPA1678, Package_SO:SOIC-8_3.9x4.9mm_P1.27mm, F.Cu at (201.8, 145.5)
- added U1302: TS12A12511, Package_SO:MSOP-8_3x3mm_P0.65mm, F.Cu at (209.7, 144.5)
- added U1401: TS12A12511, Package_SO:MSOP-8_3x3mm_P0.65mm, F.Cu at (116.2, 217.5)
- added U2201: OPA1678, Package_SO:SOIC-8_3.9x4.9mm_P1.27mm, F.Cu at (210.2, 227.0)
- added U2301: TS12A12511, Package_SO:MSOP-8_3x3mm_P0.65mm, F.Cu at (97.3, 217.5)
- added U2401: NJM4556A, Package_SO:SOIC-8_3.9x4.9mm_P1.27mm, F.Cu at (228.8, 82.6)
- added U2402: OPA1678, Package_SO:SOIC-8_3.9x4.9mm_P1.27mm, F.Cu at (228.8, 89.2)
- added U2403: NJM4556A, Package_SO:SOIC-8_3.9x4.9mm_P1.27mm, F.Cu at (228.8, 95.8)
- added U3101: ADP7142AUJZ-5.0, Package_TO_SOT_SMD:TSOT-23-5, F.Cu at (67.4, 221.7)
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
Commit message: Place every footprint on its board; panel parts on their edges
tools/place_panel.py, rerunnable: each footprint goes to the board its
sheet path names; the 25 panel parts take their x from the panel
drawings (front mirrored, rear as drawn), are turned so the side where
the courtyard overhangs the pads -- the nose -- faces the panel, and
sit with pads 2 mm inside the edge; the four ribbon headers lie along
the V-cut edges (front/control pair at x=40, control/rear at x=260);
everything else is spread row-major per sub-sheet inside its board,
clear of the edge zones, as a starting point for hand layout.  Min
through drill 0.2 mm (the TPS7A4701 thermal-via footprint).
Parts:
- moved J3202 269.1 mm to (289.8, 233.8), turned to -90 degrees
- moved SW3201 239.8 mm to (238.0, 234.0), turned to 180 degrees
- moved SW3203 236.2 mm to (251.0, 234.0), turned to 180 degrees
- moved C2001 226.4 mm to (14.3, 67.2)
- moved C2301 225.5 mm to (284.5, 97.9)
- moved U1302 222.7 mm to (15.2, 36.0)
- moved C2002 222.5 mm to (20.0, 67.2)
- moved C2003 218.8 mm to (25.6, 67.2)
- moved J3201 217.2 mm to (264.8, 248.7), turned to 180 degrees
- moved J1001 210.4 mm to (204.9, 2.90)
- moved R1401 208.8 mm to (24.9, 34.9)
- moved C1401 208.3 mm to (20.9, 34.9)
- moved R2418 205.8 mm to (17.5, 97.9)
- moved R3210 205.4 mm to (272.5, 194.8)
- moved R2417 205.0 mm to (13.5, 97.9)
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
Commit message: Supply moves to the control board; rear board deepened to 90 mm
The rear board was 2.7x denser than the control board and nothing tied
the supply to the rear panel once the Powerpole became a pigtail.  The
Supply sheet now sits under the Control Board sheet (page 25, refs
31xx -> 25xx by table, mentions renamed the same way); the pigtail
lands on the control board's JST; BIAS_5V takes ribbon pin 2 (the bias
switches stay on the rear) and RAW_13V8 leaves the ribbon.  Netlist
otherwise identical.  Panel is now 300 x 270 (REAR 90 deep); harness
and power tree regenerated; drawings and DESIGN updated.

The PCB still holds the supply footprints under their old paths: next
Update PCB from Schematic re-links them, then place_panel --all.
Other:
- board size 300 x 250 mm -> 300 x 270 mm
- board text added: "TBOX REAR BOARD rev 0.2 (300 x 90)"
- board text added: "TBox panel: 300 x 270, 4-layer 1.6 mm, two V-scores; snap apart into FRONT / CONTROL / REAR"
- board text removed: "TBOX REAR BOARD rev 0.2 (300 x 70)"
- board text removed: "TBox panel: 300 x 250, 4-layer 1.6 mm, two V-scores; snap apart into FRONT / CONTROL / REAR"
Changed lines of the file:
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@@
 	)
 	(gr_line
-		(start 0 250)
+		(start 0 270)
 		(end 0 0)
 		(stroke
@@
 	(gr_line
 		(start 300 0)
-		(end 300 250)
+		(end 300 270)
 		(stroke
 			(width 0.1)
@@
 	)
 	(gr_line
-		(start 300 250)
-		(end 0 250)
+		(start 300 270)
+		(end 0 270)
 		(stroke
 			(width 0.1)
@@
 	)
 	(gr_text "panel edge / jacks"
-		(at 150 244 0)
+		(at 150 264 0)
 		(layer "Cmts.User")
 		(effects
@@
 		)
 	)
-	(gr_text "TBox panel: 300 x 250, 4-layer 1.6 mm, two V-scores; snap apart into FRONT / CONTROL / REAR"
+	(gr_text "TBox panel: 300 x 270, 4-layer 1.6 mm, two V-scores; snap apart into FRONT / CONTROL / REAR"
 		(at 6 -4 0)
 		(layer "Cmts.User")
@@
 		)
 	)
-	(gr_text "TBOX REAR BOARD  rev 0.2  (300 x 70)"
-		(at 150 215 0)
+	(gr_text "TBOX REAR BOARD  rev 0.2  (300 x 90)"
+		(at 150 225 0)
 		(layer "Cmts.User")
 		(effects
@@
 	)
 	(group "panel-frame"
-		(members "0d36ca59-829b-4d05-8a1c-c1171b89385f" "0ef4c589-dbb9-407e-b9ce-cbe3d9ea344b"
-			"31acdba0-88ae-45a2-8159-f006ab0dd3bf" "3faef886-778b-4d7f-ab93-321de16bfd87"
-			"422f5b66-64d1-4b97-9932-e352fd040489" "7573f696-e1d9-4654-a22c-b12126bd998d"
-			"806d2466-e265-484b-87ed-be4dc60192a9" "86f1abd8-1cc2-4511-a3ce-a3d52baed64d"
-			"9034c051-0bd3-4af7-bf9c-432e813ae289" "907fdb43-cc04-4288-9121-672c6a5c5cd9"
-			"9ed37533-721f-44b9-9d3d-697c74341964" "bc986294-5114-495f-8240-80dfdc6fc1ff"
-			"d425fddc-a716-4a0e-bccd-20731b594781" "eee2166e-1dce-4c44-82d4-4d0a440fa344"
-			"f702d4cc-b69d-4701-b3c4-a39cd40881b3"
+		(members "234988ed-7228-4fdb-bde6-a7086995d15b" "24a6d0ee-06de-4ff1-a655-c7941ca80672"
+			"3d3182f1-283a-41f2-ad61-9f85751f0785" "4cb3b099-3fe9-4b38-998d-e6823aa51a9b"
+			"5832edc0-29b6-4240-b942-0f0a5cd7df61" "689919cf-bed2-43f4-a995-457159a78be0"
+			"7b11ba20-4bb4-4df2-bf14-fb631740e1f6" "7c7da980-d93d-443f-8455-f2a9935174d3"
+			"7c7e08be-1c1a-4d4c-bfe8-965a6fe54e2f" "bad71623-b0e1-4758-aed5-2628347126c9"
+			"da93888e-40fe-4a29-91da-7a4ec4e2f3a1" "dce50c41-6b22-4afe-a2e6-4994a6d10086"
+			"e96f85b0-0990-46dc-8784-37e458dd36b1" "eed6b565-a2a4-4017-8594-8f593ee69b07"
+			"fabbdb59-e8f0-41be-aa89-74eab2f37789"
 		)
 	)
